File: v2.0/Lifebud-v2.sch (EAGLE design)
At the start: 47 parts, among them IC1 MCP73831/OT, Q1 BSS138, Q2 BSS138, Q3 BSS138, U2 MIC5219 3.3V, U3 MMA8452Q, U4 FT232RL, Y1 32.768kHz

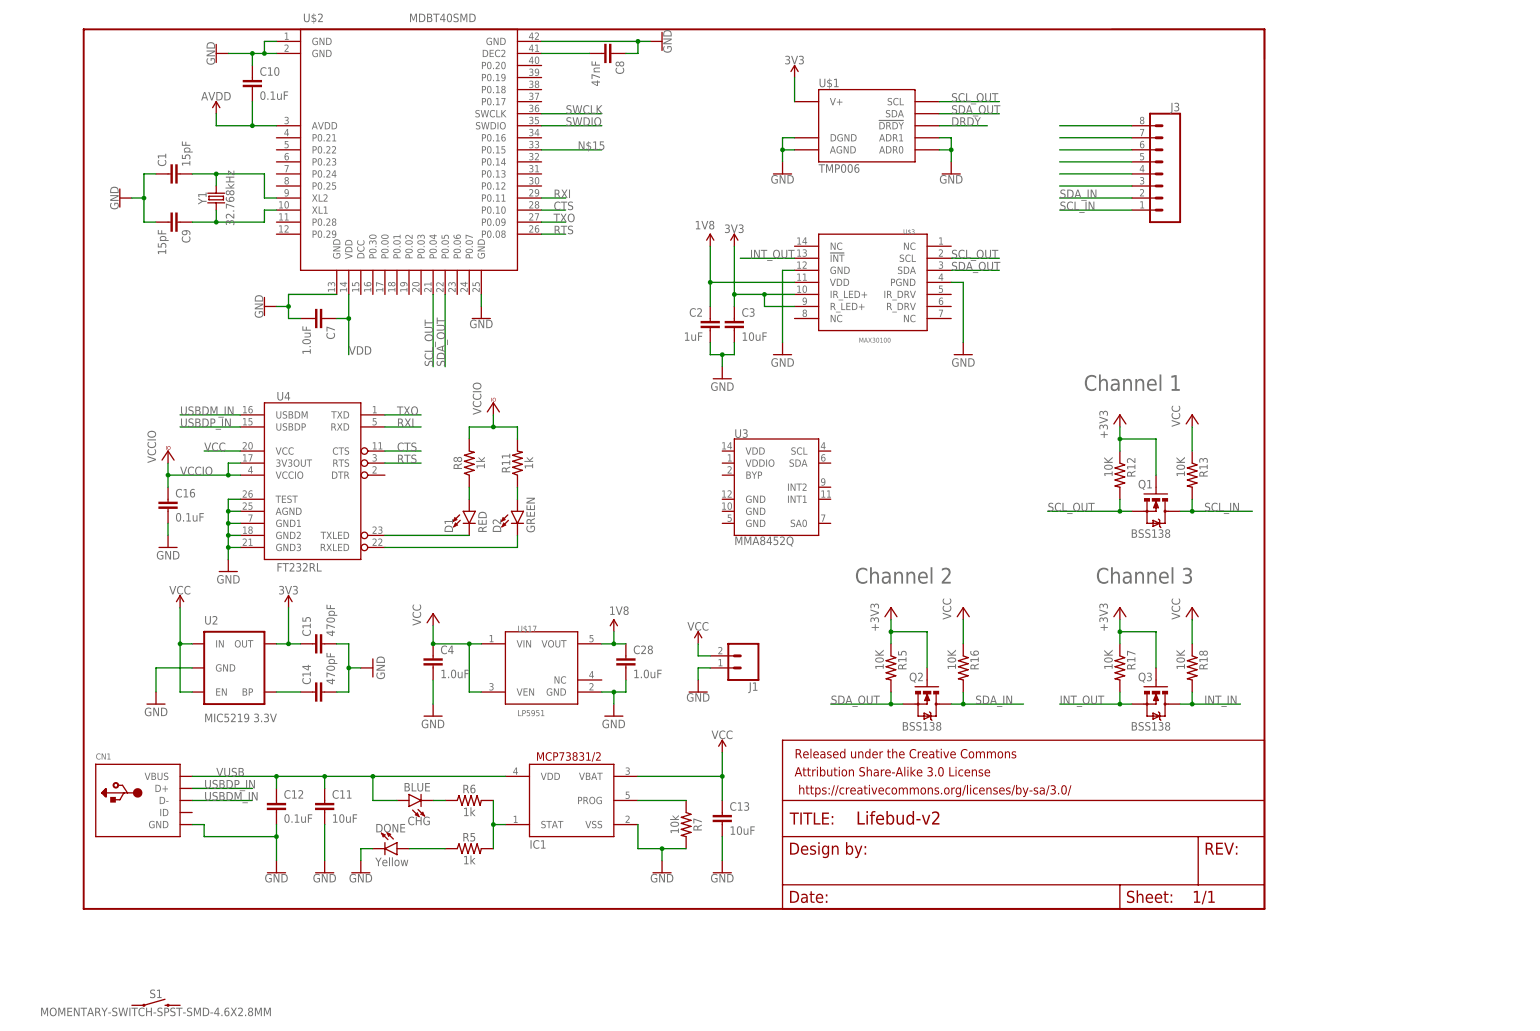
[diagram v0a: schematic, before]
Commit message: nearly finished with the DC/DC converter setup on nrf51
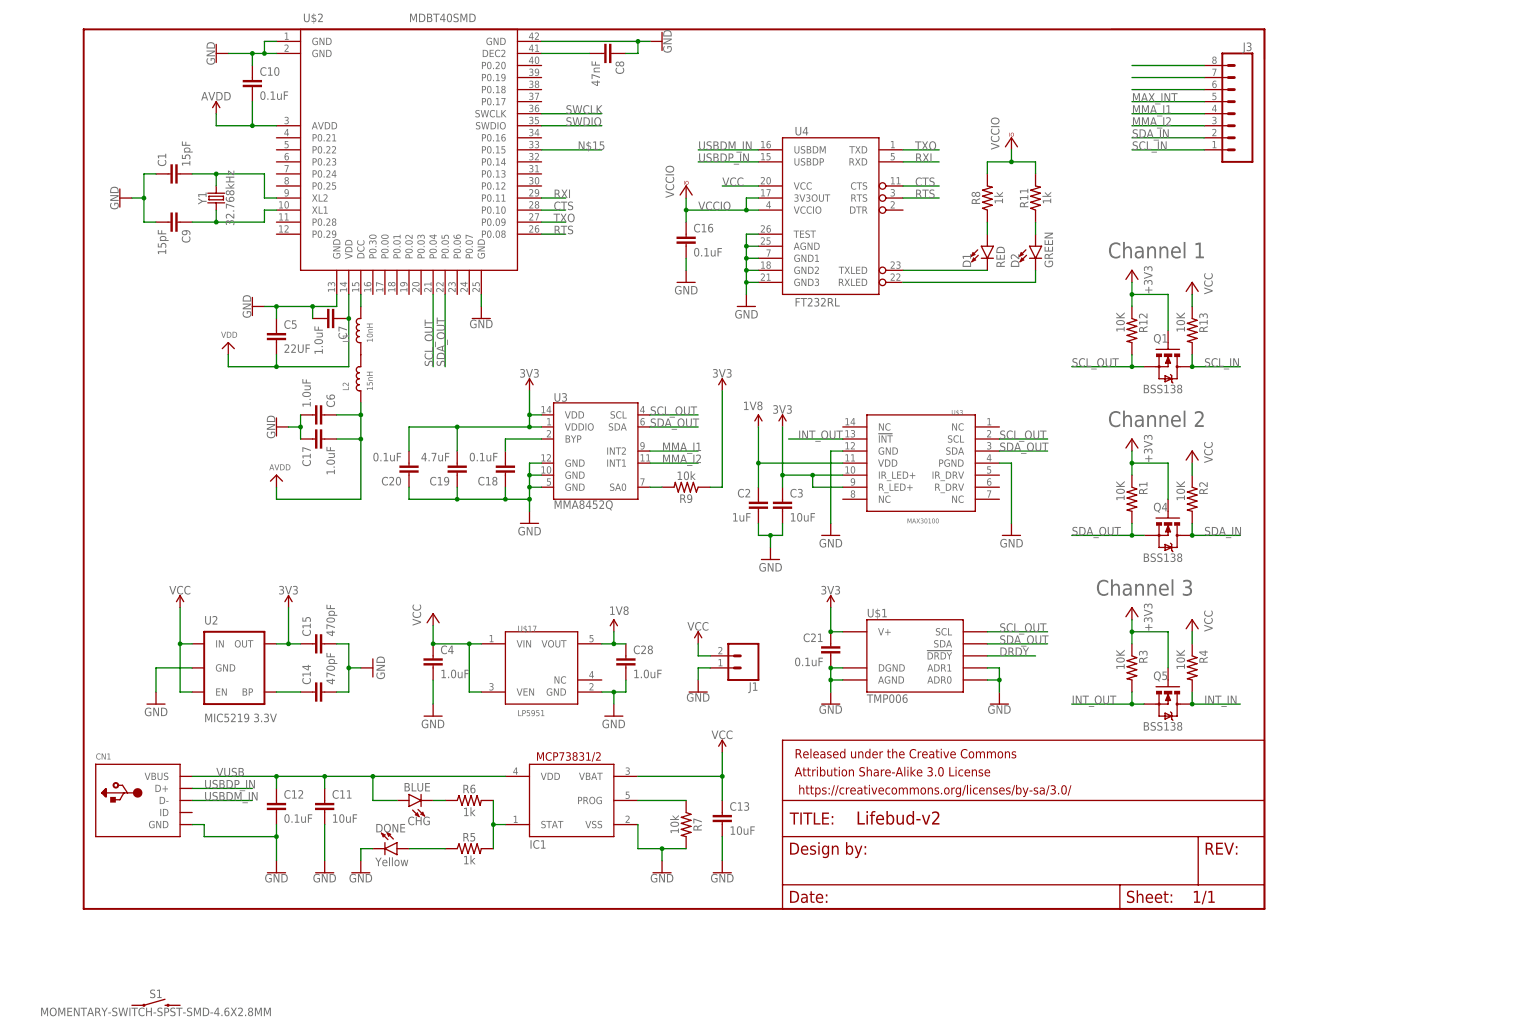
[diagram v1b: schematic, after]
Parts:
- removed Q2, Q3: BSS138, SparkFun:MOSFET-NCHANNELSMD
- removed R15, R16, R17: 10K, SparkFun:RESISTOR0402-RES
- added C17, C6: 1.0uF, SparkFun-Capacitors:1.0UF-0603-16V-10%
- added C18, C20, C21: 0.1uF, SparkFun-Capacitors:0.1UF-0402-16V-10%
- added C19: 4.7uF, SparkFun-Capacitors:4.7UF0603
- added C5: 22UF, SparkFun-Capacitors:22UF-1210-16V-20%
- added L1: 10nH, microbuilder:INDUCTOR0603
- added L2: 15nH, microbuilder:INDUCTOR0603
- added Q4, Q5: BSS138, SparkFun:MOSFET-NCHANNELSMD
- added R1, R2, R3: 10K, SparkFun:RESISTOR0402-RES
- added R9: 10k, SparkFun-Resistors:10KOHM-0603-1/10W-1%
- renumbered R18 to R4
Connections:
- net N$17 renamed MAX_INT
- removed net N$18: J3.4
- removed net N$19: J3.3
- new net AVDD: C17.2, C6.1, L2.1
- new net MMA_I1: J3.4, U3.INT2
- new net MMA_I2: J3.3, U3.INT1
- new net N$20: L1.1, L2.2
- new net N$22: L1.2, U$2.DCC
- new net N$24: C18.2, U3.BYP
- new net N$25: R9.2, U3.SA0
- net +3V3: now also Q4.G, Q5.G, R1.1, R3.1; no longer Q2.G, Q3.G, R15.1, R17.1
- net 3V3: no longer U$1.V+
- net GND: now also C17.1, C18.1, C19.1, C20.1, C21.2, C5.1, C6.2, U3.GND@0, U3.GND@1, U3.GND@2
- net INT_IN: now also Q5.D; no longer Q3.D
- net INT_OUT: now also Q5.S, R3.2; no longer Q3.S, R17.2
- net SCL_OUT: now also U3.SCL
- net SDA_IN: now also Q4.D, R2.2; no longer Q2.D, R16.2
- net SDA_OUT: now also Q4.S, R1.2, U3.SDA; no longer Q2.S, R15.2
- net VCC: now also C19.2, C20.2, C21.1, R2.1, R9.1, U$1.V+, U3.VDD, U3.VDDIO; no longer R16.1
- net VDD: now also C5.2
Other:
- moved on the sheet: C16, C2, C3, C7, D1, D2, J3, Q1, R11, R12, R13, R8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

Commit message: cleaned up schematic, need to check for errors with ERC
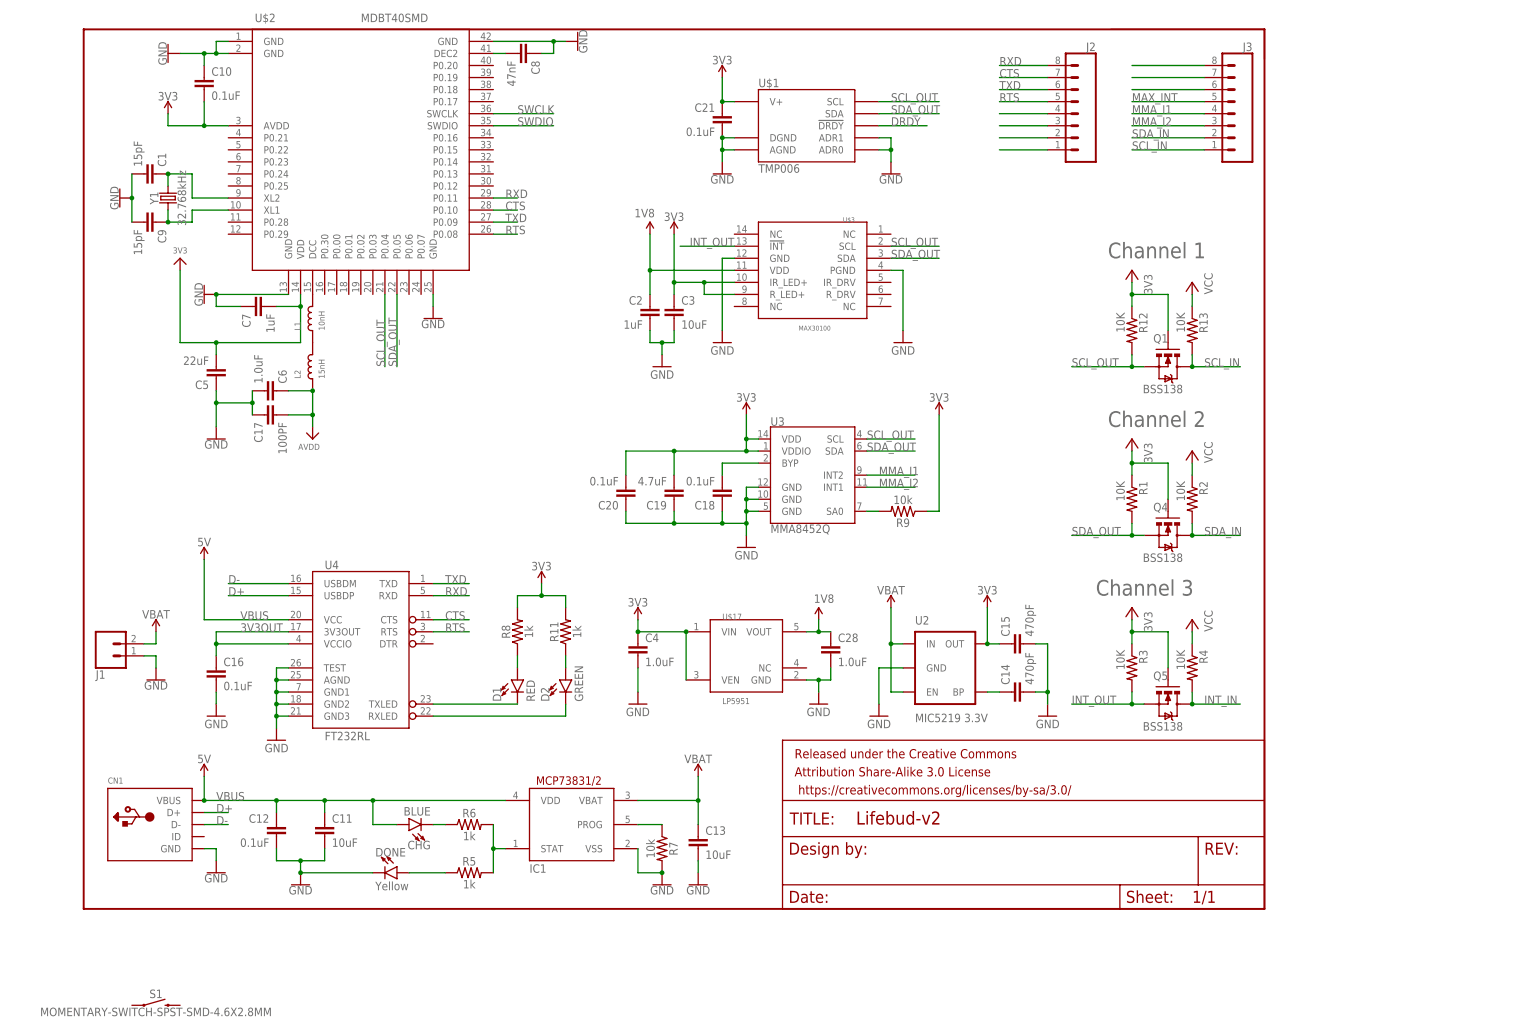
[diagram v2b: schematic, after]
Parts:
- added J2: (no value), SparkFun-Connectors:CONN_08"
- C17: value 1.0uF -> 100PF; device SparkFun-Capacitors:1.0UF-0603-16V-10% -> SparkFun-Capacitors:100PF-0402-50V-5%
- C5: value 22UF -> 22uF; device SparkFun-Capacitors:22UF-1210-16V-20% -> SparkFun-Capacitors:22UF-0805-6.3V-20%
- C7: value 1.0uF -> 1uF
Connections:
- net USBDM_IN renamed D-
- net USBDP_IN renamed D+
- removed net +3V3: Q1.G, Q4.G, Q5.G, R1.1, R12.1, R3.1
- removed net N$15: U$2.P0.15
- removed net RXI: U$2.P0.11, U4.RXD
- removed net TXO: U$2.P0.09, U4.TXD
- removed net VCC: C10.2, C13.1, C19.2, C20.2, C21.1, C4.1, IC1.VBAT, J1.1, R13.1, R2.1, R4.1, R9.1, U$1.V+, U$17.VEN, U$17.VIN, U$2.AVDD, U2.EN, U2.IN, U3.VDD, U3.VDDIO, U4.VCC
- removed net VCCIO: C16.1, R11.2, R8.2, U4.3V3OUT, U4.VCCIO
- removed net VDD: C5.2, C7.1, U$2.VDD
- removed net VUSB: C11.1, C12.1, CHG.A, CN1.VBUS, IC1.VDD
- new net 3V3OUT: C16.1, U4.3V3OUT, U4.VCCIO
- new net N$23: J2.4
- new net N$26: J2.3
- new net N$27: J2.2
- new net N$28: J2.1
- new net RXD: J2.8, U$2.P0.11, U4.RXD
- new net TXD: J2.6, U$2.P0.09, U4.TXD
- new net VBAT: C13.1, C19.2, C20.2, C21.1, IC1.VBAT, J1.1, R13.1, R2.1, R4.1, R9.1, U$1.V+, U2.EN, U2.IN, U3.VDD, U3.VDDIO
- new net VBUS: C11.1, C12.1, CHG.A, CN1.VBUS, IC1.VDD, U4.VCC
- net 3V3: now also C10.2, C4.1, C5.2, C7.2, Q1.G, Q4.G, Q5.G, R1.1, R11.2, R12.1, R3.1, R8.2, U$17.VEN, U$17.VIN, U$2.AVDD, U$2.VDD
- net CTS: now also J2.7
- net GND: now also C1.2, C7.1; no longer C1.1, C7.2
- net N$4: now also C1.1; no longer C1.2
- net RTS: now also J2.5
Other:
- moved on the sheet: C1, C10, C11, C12, C13, C14, C15, C16, C17, C18, C19, C2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

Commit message: organized components using the line tool
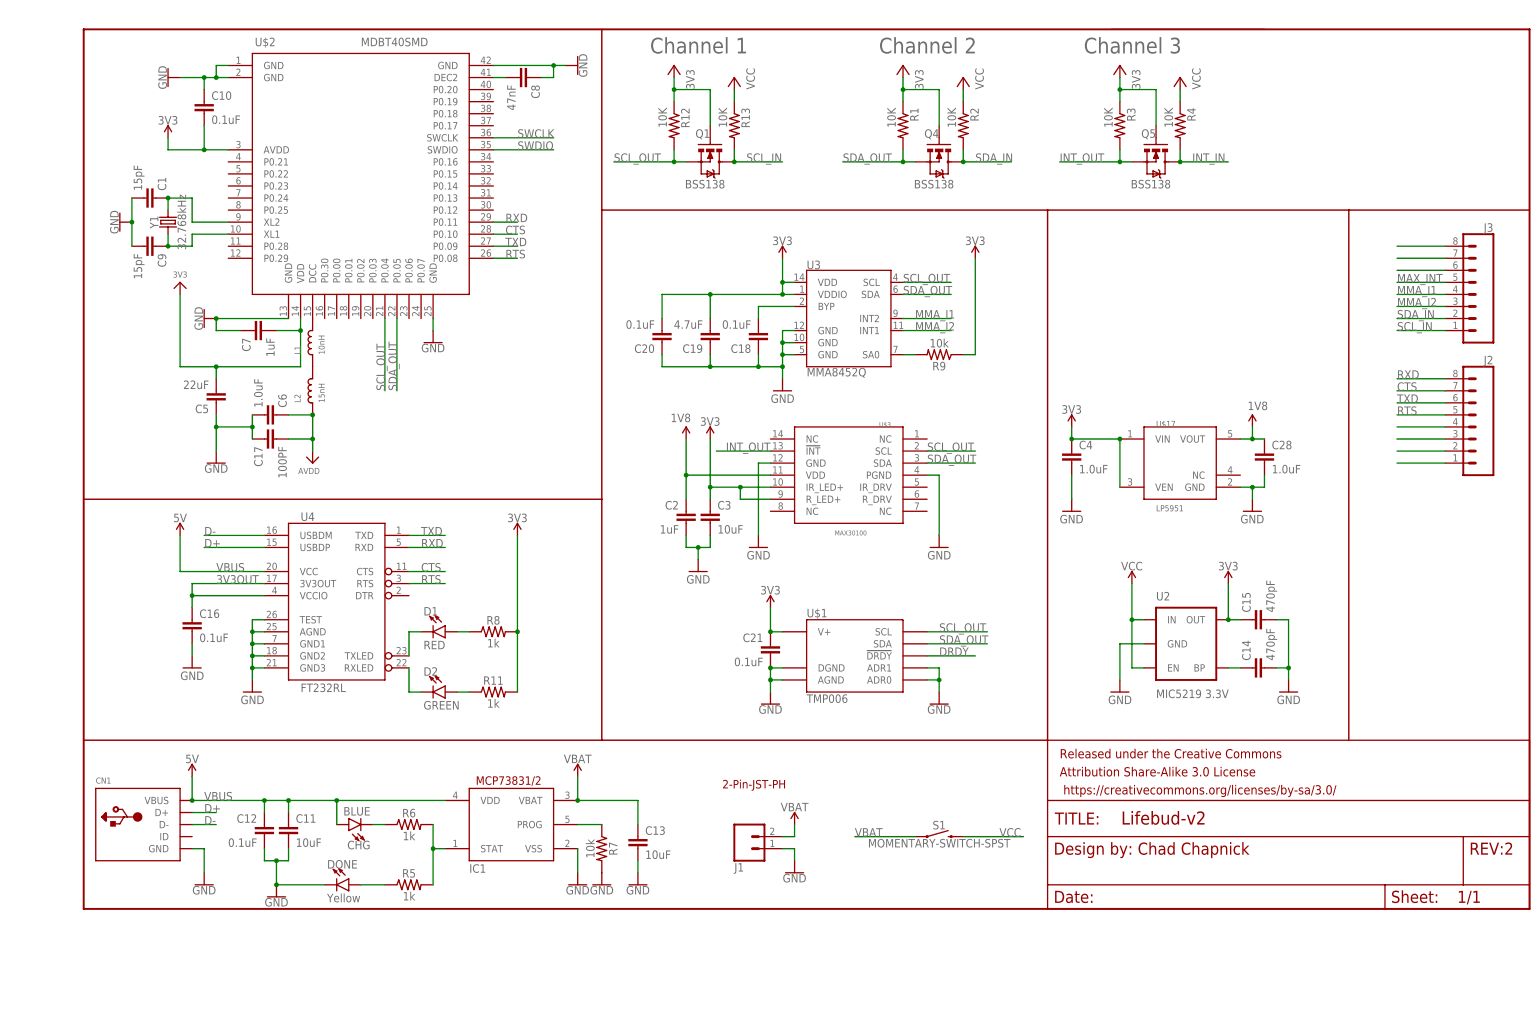
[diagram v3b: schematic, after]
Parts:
- S1: value MOMENTARY-SWITCH-SPST-SMD-4.6X2.8MM -> MOMENTARY-SWITCH-SPST
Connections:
- new net VCC: C19.2, C20.2, C21.1, R13.1, R2.1, R4.1, R9.1, S1.2, U$1.V+, U2.EN, U2.IN, U3.VDD, U3.VDDIO
- net VBAT: now also S1.1; no longer C19.2, C20.2, C21.1, R13.1, R2.1, R4.1, R9.1, U$1.V+, U2.EN, U2.IN, U3.VDD, U3.VDDIO
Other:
- note added: "2-Pin-JST-PH"
- moved on the sheet: C1, C10, C11, C12, C13, C14, C15, C16, C17, C18, C19, C2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
